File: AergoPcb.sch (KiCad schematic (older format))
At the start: 16 parts, among them SW1 SW_Push, U1 ATmega32U4-AU, Y1 16MHz

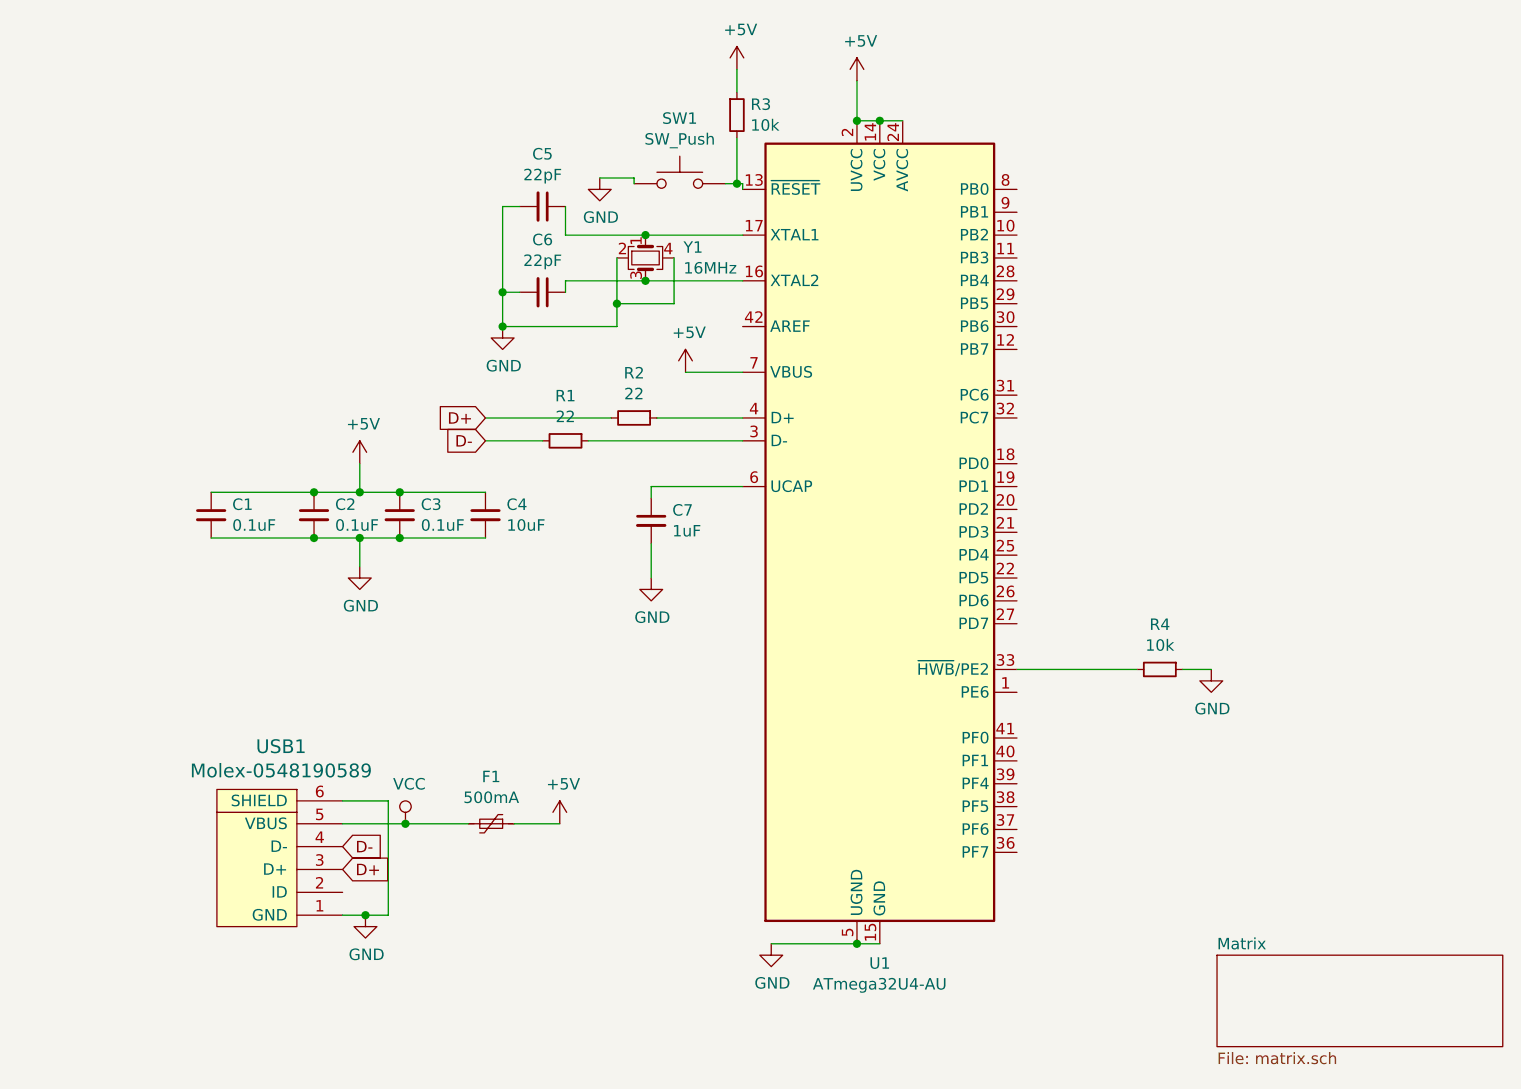
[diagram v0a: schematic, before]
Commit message: added jst footprints, continued work on pcb
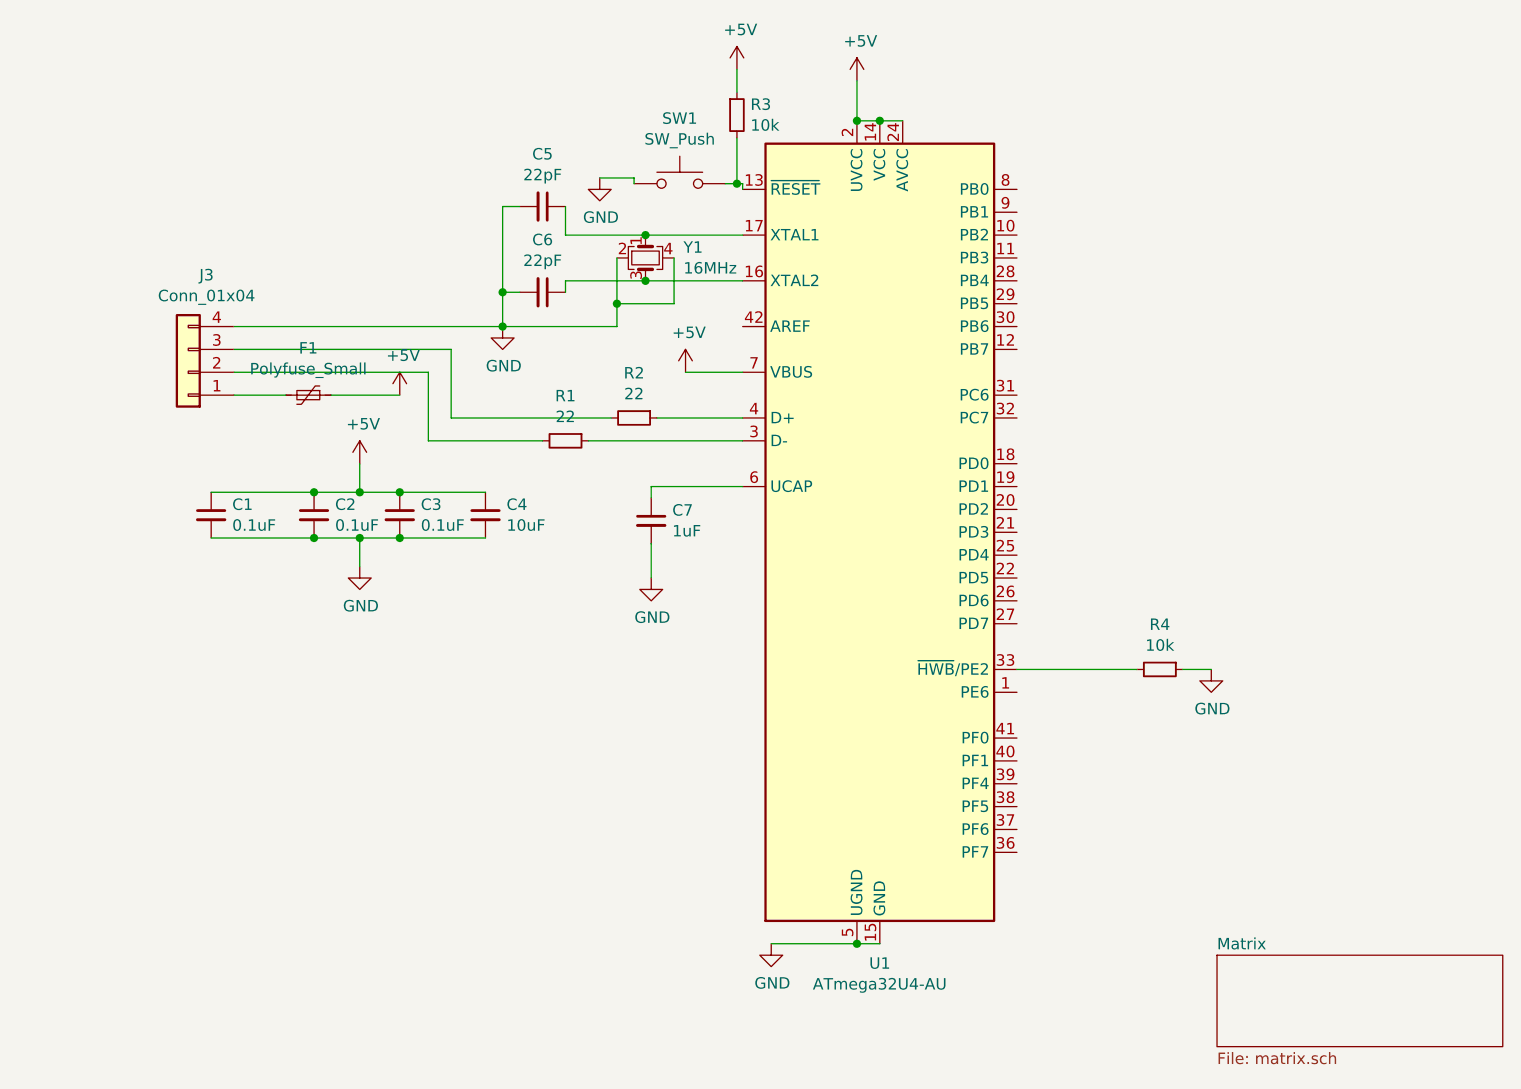
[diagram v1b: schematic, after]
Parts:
- removed USB1: Molex-0548190589, symbol random-keyboard-parts:Molex-0548190589
- added J3: Conn_01x04, symbol Connector_Generic:Conn_01x04
- C1, C2, C3, C4, C5, C6, C7: footprint (none) -> Capacitor_SMD:C_0805_2012Metric
- F1: value 500mA -> Polyfuse_Small
- R1, R2, R3, R4: footprint (none) -> Resistor_SMD:R_0805_2012Metric
- SW1: footprint (none) -> random-keyboard-parts:SKQG-1155865
- Y1: footprint (none) -> Crystal:Crystal_SMD_3225-4Pin_3.2x2.5mm
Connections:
- net GND: now also J3.4 (Pin_4)
- net D+: no longer names the net of R2.2
- net D+: now also J3.3 (Pin_3)
- net D-: no longer names the net of R1.2
- net D-: now also J3.2 (Pin_2)
- net VCC: no longer names the net of F1.2
- net VCC: now also J3.1 (Pin_1)
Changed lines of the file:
@@
 F 0 "R4" V 5329 4225 50  0000 C CNN
 F 1 "10k" V 5420 4225 50  0000 C CNN
-F 2 "" H 5525 4225 50  0001 C CNN
+F 2 "Resistor_SMD:R_0805_2012Metric" H 5525 4225 50  0001 C CNN
 F 3 "~" H 5525 4225 50  0001 C CNN
 	1    5525 4225
@@
 F 0 "R2" V 3029 3125 50  0000 C CNN
 F 1 "22" V 3120 3125 50  0000 C CNN
-F 2 "" H 3225 3125 50  0001 C CNN
+F 2 "Resistor_SMD:R_0805_2012Metric" H 3225 3125 50  0001 C CNN
 F 3 "~" H 3225 3125 50  0001 C CNN
 	1    3225 3125
@@
 F 0 "R1" V 2729 3225 50  0000 C CNN
 F 1 "22" V 2820 3225 50  0000 C CNN
-F 2 "" H 2925 3225 50  0001 C CNN
+F 2 "Resistor_SMD:R_0805_2012Metric" H 2925 3225 50  0001 C CNN
 F 3 "~" H 2925 3225 50  0001 C CNN
 	1    2925 3225
@@
 Wire Wire Line
 	3700 3125 3325 3125
-Wire Wire Line
-	2825 3225 2575 3225
-Wire Wire Line
-	3125 3125 2575 3125
 $Comp
 L Device:C_Small C7
@@
 F 0 "C7" H 3392 3621 50  0000 L CNN
 F 1 "1uF" H 3392 3530 50  0000 L CNN
-F 2 "" H 3300 3575 50  0001 C CNN
+F 2 "Capacitor_SMD:C_0805_2012Metric" H 3300 3575 50  0001 C CNN
 F 3 "~" H 3300 3575 50  0001 C CNN
 	1    3300 3575
@@
 F 0 "C1" H 1467 3596 50  0000 L CNN
 F 1 "0.1uF" H 1467 3505 50  0000 L CNN
-F 2 "" H 1375 3550 50  0001 C CNN
+F 2 "Capacitor_SMD:C_0805_2012Metric" H 1375 3550 50  0001 C CNN
 F 3 "~" H 1375 3550 50  0001 C CNN
 	1    1375 3550
@@
 F 0 "C2" H 1917 3596 50  0000 L CNN
 F 1 "0.1uF" H 1917 3505 50  0000 L CNN
-F 2 "" H 1825 3550 50  0001 C CNN
+F 2 "Capacitor_SMD:C_0805_2012Metric" H 1825 3550 50  0001 C CNN
 F 3 "~" H 1825 3550 50  0001 C CNN
 	1    1825 3550
@@
 F 0 "C3" H 2292 3596 50  0000 L CNN
 F 1 "0.1uF" H 2292 3505 50  0000 L CNN
-F 2 "" H 2200 3550 50  0001 C CNN
+F 2 "Capacitor_SMD:C_0805_2012Metric" H 2200 3550 50  0001 C CNN
 F 3 "~" H 2200 3550 50  0001 C CNN
 	1    2200 3550
@@
 F 0 "C4" H 2667 3596 50  0000 L CNN
 F 1 "10uF" H 2667 3505 50  0000 L CNN
-F 2 "" H 2575 3550 50  0001 C CNN
+F 2 "Capacitor_SMD:C_0805_2012Metric" H 2575 3550 50  0001 C CNN
 F 3 "~" H 2575 3550 50  0001 C CNN
 	1    2575 3550
@@
 Wire Wire Line
 	2025 3650 2200 3650
-Wire Wire Line
-	2025 3450 2025 3325
 Connection ~ 2025 3450
 Wire Wire Line
@@
 F 0 "Y1" V 3229 2591 50  0000 L CNN
 F 1 "16MHz" V 3320 2591 50  0000 L CNN
-F 2 "" H 3275 2425 50  0001 C CNN
+F 2 "Crystal:Crystal_SMD_3225-4Pin_3.2x2.5mm" H 3275 2425 50  0001 C CNN
 F 3 "~" H 3275 2425 50  0001 C CNN
 	1    3275 2425
@@
 F 0 "C5" V 2596 2200 50  0000 C CNN
 F 1 "22pF" V 2687 2200 50  0000 C CNN
-F 2 "" H 2825 2200 50  0001 C CNN
+F 2 "Capacitor_SMD:C_0805_2012Metric" H 2825 2200 50  0001 C CNN
 F 3 "~" H 2825 2200 50  0001 C CNN
 	1    2825 2200
@@
 F 0 "C6" V 2596 2575 50  0000 C CNN
 F 1 "22pF" V 2687 2575 50  0000 C CNN
-F 2 "" H 2825 2575 50  0001 C CNN
+F 2 "Capacitor_SMD:C_0805_2012Metric" H 2825 2575 50  0001 C CNN
 F 3 "~" H 2825 2575 50  0001 C CNN
 	1    2825 2575
@@
 F 0 "SW1" H 3425 2385 50  0000 C CNN
 F 1 "SW_Push" H 3425 2294 50  0000 C CNN
-F 2 "" H 3425 2300 50  0001 C CNN
+F 2 "random-keyboard-parts:SKQG-1155865" H 3425 2300 50  0001 C CNN
 F 3 "" H 3425 2300 50  0001 C CNN
 	1    3425 2100
@@
 F 0 "R3" H 3734 1846 50  0000 L CNN
 F 1 "10k" H 3734 1755 50  0000 L CNN
-F 2 "" H 3675 1800 50  0001 C CNN
+F 2 "Resistor_SMD:R_0805_2012Metric" H 3675 1800 50  0001 C CNN
 F 3 "~" H 3675 1800 50  0001 C CNN
 	1    3675 1800
@@
 	1    0    0    -1
 $EndComp
-Wire Wire Line
-	3675 1700 3675 1600
-Text GLabel 2575 3125 0    50   Input ~ 0
-D+
-Text GLabel 2575 3225 0    50   Input ~ 0
-D-
-$Comp
-L random-keyboard-parts:Molex-0548190589 USB1
-U 1 1 5C859DAB
-P 1650 5100
-F 0 "USB1" V 2187 5069 60  0000 C CNN
-F 1 "Molex-0548190589" V 2081 5069 60  0000 C CNN
-F 2 "" H 1650 5100 60  0001 C CNN
-F 3 "" H 1650 5100 60  0001 C CNN
-	1    1650 5100
-	0    -1   -1   0
-$EndComp
-$Comp
-L Device:Polyfuse_Small F1
-U 1 1 5C859EB2
-P 2600 4900
-F 0 "F1" V 2395 4900 50  0000 C CNN
-F 1 "500mA" V 2486 4900 50  0000 C CNN
-F 2 "" H 2650 4700 50  0001 L CNN
-F 3 "~" H 2600 4900 50  0001 C CNN
-	1    2600 4900
-	0    1    1    0
-$EndComp
-$Comp
-L power:VCC #PWR04
-U 1 1 5C85ABBD
-P 2225 4900
-F 0 "#PWR04" H 2225 4750 50  0001 C CNN
-F 1 "VCC" H 2242 5073 50  0000 C CNN
-F 2 "" H 2225 4900 50  0001 C CNN
-F 3 "" H 2225 4900 50  0001 C CNN
-	1    2225 4900
-	1    0    0    -1
-$EndComp
-$Comp
-L power:+5V #PWR06
-U 1 1 5C85AC52
-P 2900 4900
-F 0 "#PWR06" H 2900 4750 50  0001 C CNN
-F 1 "+5V" H 2915 5073 50  0000 C CNN
-F 2 "" H 2900 4900 50  0001 C CNN
-F 3 "" H 2900 4900 50  0001 C CNN
-	1    2900 4900
-	1    0    0    -1
-$EndComp
-Text GLabel 1950 5100 2    50   Input ~ 0
-D+
-Text GLabel 1950 5000 2    50   Input ~ 0
-D-
-Wire Wire Line
-	1950 4900 2225 4900
-Wire Wire Line
-	2225 4900 2500 4900
-Connection ~ 2225 4900
-Wire Wire Line
-	2700 4900 2900 4900
-$Comp
-L power:GND #PWR03
-U 1 1 5C85FBAF
-P 2050 5300
-F 0 "#PWR03" H 2050 5050 50  0001 C CNN
-F 1 "GND" H 2055 5127 50  0000 C CNN
-F 2 "" H 2050 5300 50  0001 C CNN
-F 3 "" H 2050 5300 50  0001 C CNN
-	1    2050 5300
-	1    0    0    -1
-$EndComp
-Wire Wire Line
-	1950 5300 2050 5300
 $Sheet
 S 5775 5475 1250 400
@@
 	1    0    0    -1
 $EndComp
-Wire Wire Line
-	1950 4800 2150 4800
-Wire Wire Line
-	2150 4800 2150 5300
-Wire Wire Line
-	2150 5300 2050 5300
-Connection ~ 2050 5300
+$Comp
+L Connector_Generic:Conn_01x04 J3
+U 1 1 5C95CF30
+P 1275 2925
+F 0 "J3" H 1195 2500 50  0000 C CNN
+F 1 "Conn_01x04" H 1195 2591 50  0000 C CNN
+F 2 "" H 1275 2925 50  0001 C CNN
+F 3 "~" H 1275 2925 50  0001 C CNN
+	1    1275 2925
+	-1   0    0    1
+$EndComp
+Wire Wire Line
+	2325 3225 2825 3225
+Wire Wire Line
+	3675 1600 3675 1700
+Wire Wire Line
+	2325 3225 2325 2925
+Wire Wire Line
+	2425 3125 2425 2825
+Wire Wire Line
+	2425 3125 3125 3125
+$Comp
+L Device:Polyfuse_Small F1
+U 1 1 5C9AFBD1
+P 1800 3025
+F 0 "F1" V 1595 3025 50  0000 C CNN
+F 1 "Polyfuse_Small" V 1686 3025 50  0000 C CNN
+F 2 "" H 1850 2825 50  0001 L CNN
+F 3 "~" H 1800 3025 50  0001 C CNN
+	1    1800 3025
+	0    1    1    0
+$EndComp
+Wire Wire Line
+	1475 2725 2650 2725
+Wire Wire Line
+	1475 2825 2425 2825
+Wire Wire Line
+	1475 2925 2325 2925
+Wire Wire Line
+	1475 3025 1700 3025
+Wire Wire Line
+	2025 3325 2025 3450
+$Comp
+L power:+5V #PWR0101
+U 1 1 5CBAF4D0
+P 2200 3025
+F 0 "#PWR0101" H 2200 2875 50  0001 C CNN
+F 1 "+5V" H 2215 3198 50  0000 C CNN
+F 2 "" H 2200 3025 50  0001 C CNN
+F 3 "" H 2200 3025 50  0001 C CNN
+	1    2200 3025
+	1    0    0    -1
+$EndComp
+Wire Wire Line
+	1900 3025 2200 3025
 $EndSCHEMATC

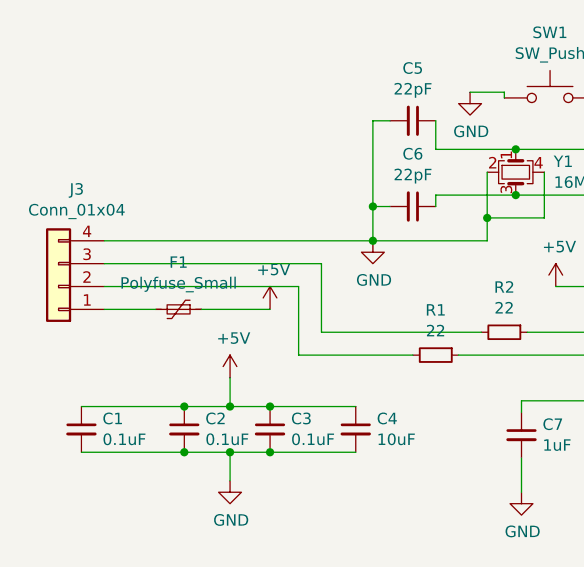
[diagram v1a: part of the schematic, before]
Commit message: finished right half, loaded keyboard parts pretty
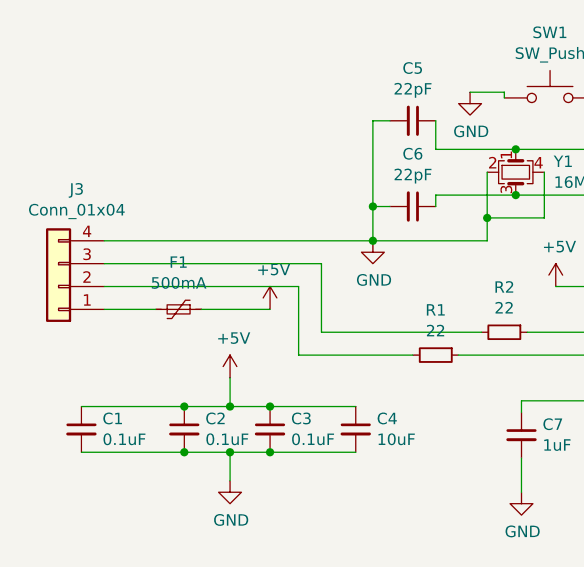
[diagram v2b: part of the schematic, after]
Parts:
- F1: value Polyfuse_Small -> 500mA; footprint (none) -> Fuse_Holders_and_Fuses:Fuse_SMD1206_Reflow
- J3: footprint (none) -> Connector_JST:JST_SH_SM04B-SRSS-TB_1x04-1MP_P1.00mm_Horizontal
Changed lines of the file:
@@
 F 0 "J3" H 1195 2500 50  0000 C CNN
 F 1 "Conn_01x04" H 1195 2591 50  0000 C CNN
-F 2 "" H 1275 2925 50  0001 C CNN
+F 2 "Connector_JST:JST_SH_SM04B-SRSS-TB_1x04-1MP_P1.00mm_Horizontal" H 1275 2925 50  0001 C CNN
 F 3 "~" H 1275 2925 50  0001 C CNN
 	1    1275 2925
@@
 P 1800 3025
 F 0 "F1" V 1595 3025 50  0000 C CNN
-F 1 "Polyfuse_Small" V 1686 3025 50  0000 C CNN
-F 2 "" H 1850 2825 50  0001 L CNN
+F 1 "500mA" V 1686 3025 50  0000 C CNN
+F 2 "Fuse_Holders_and_Fuses:Fuse_SMD1206_Reflow" H 1850 2825 50  0001 L CNN
 F 3 "~" H 1800 3025 50  0001 C CNN
 	1    1800 3025

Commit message: Finalized PCB and created Gerbers
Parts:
- added U2: PRTR5V0U2X, random-keyboard-parts:SOT143B, symbol 2019-04-04_07-10-47:PRTR5V0U2X
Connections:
- net GND: now also U2.1 (GND)
- net COL9: now reaches U1.10 (PB2)
- net COL8: now reaches U1.11 (PB3)
- net COL6: now reaches U1.19 (PD1)
- net SwLedPWM: now reaches U1.20 (PD2)
- net COL0: now reaches U1.21 (PD3)
- net ROW1: now reaches U1.22 (PD5)
- net ROW5: now reaches U1.25 (PD4)
- net COL1: now reaches U1.26 (PD6)
- net COL2: now reaches U1.27 (PD7)
- net COL3: now reaches U1.28 (PB4)
- net COL4: now reaches U1.29 (PB5)
- net D-: now reaches R1.1, U1.3 (D-)
- net ROW0: now reaches U1.30 (PB6)
- net COL5: now reaches U1.31 (PC6)
- net ROW4: now reaches U1.32 (PC7)
- net ROW3: now reaches U1.36 (PF7)
- net ROW2: now reaches U1.37 (PF6)
- net COL7: now reaches U1.38 (PF5)
- net COL13: now reaches U1.39 (PF4)
- net D+: now reaches R2.1, U1.4 (D+)
- net COL12: now reaches U1.40 (PF1)
- net COL11: now reaches U1.41 (PF0)
- net COL10: now reaches U1.9 (PB1)
- net at J3.3 (Pin_3), R2.2: now also U2.2 (I/O1)
- net at J3.2 (Pin_2), R1.2: now also U2.3 (I/O2)
- net at F1.2, J3.1 (Pin_1): now also U2.4 (VCC)
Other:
- moved on the sheet: R1, R2
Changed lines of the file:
@@
 L Device:R_Small R2
 U 1 1 5C80D3A9
-P 3225 3125
-F 0 "R2" V 3029 3125 50  0000 C CNN
-F 1 "22" V 3120 3125 50  0000 C CNN
-F 2 "Resistor_SMD:R_0805_2012Metric" H 3225 3125 50  0001 C CNN
-F 3 "~" H 3225 3125 50  0001 C CNN
-	1    3225 3125
+P 2040 2825
+F 0 "R2" V 1844 2825 50  0000 C CNN
+F 1 "22" V 1935 2825 50  0000 C CNN
+F 2 "Resistor_SMD:R_0805_2012Metric" H 2040 2825 50  0001 C CNN
+F 3 "~" H 2040 2825 50  0001 C CNN
+	1    2040 2825
 	0    1    1    0
 $EndComp
@@
 L Device:R_Small R1
 U 1 1 5C80D430
-P 2925 3225
-F 0 "R1" V 2729 3225 50  0000 C CNN
-F 1 "22" V 2820 3225 50  0000 C CNN
-F 2 "Resistor_SMD:R_0805_2012Metric" H 2925 3225 50  0001 C CNN
-F 3 "~" H 2925 3225 50  0001 C CNN
-	1    2925 3225
-	0    1    1    0
-$EndComp
-Wire Wire Line
-	3700 3225 3025 3225
-Wire Wire Line
-	3700 3125 3325 3125
+P 2040 2925
+F 0 "R1" V 1844 2925 50  0000 C CNN
+F 1 "22" V 1935 2925 50  0000 C CNN
+F 2 "Resistor_SMD:R_0805_2012Metric" H 2040 2925 50  0001 C CNN
+F 3 "~" H 2040 2925 50  0001 C CNN
+	1    2040 2925
+	0    1    1    0
+$EndComp
 $Comp
 L Device:C_Small C7
@@
 $EndComp
 Wire Wire Line
-	2325 3225 2825 3225
-Wire Wire Line
 	3675 1600 3675 1700
-Wire Wire Line
-	2325 3225 2325 2925
-Wire Wire Line
-	2425 3125 2425 2825
-Wire Wire Line
-	2425 3125 3125 3125
 $Comp
 L Device:Polyfuse_Small F1
@@
 	1475 2725 2650 2725
 Wire Wire Line
-	1475 2825 2425 2825
-Wire Wire Line
-	1475 2925 2325 2925
-Wire Wire Line
-	1475 3025 1700 3025
+	1475 3025 1585 3025
 Wire Wire Line
 	2025 3325 2025 3450
@@
 L power:+5V #PWR0101
 U 1 1 5CBAF4D0
-P 2200 3025
-F 0 "#PWR0101" H 2200 2875 50  0001 C CNN
-F 1 "+5V" H 2215 3198 50  0000 C CNN
-F 2 "" H 2200 3025 50  0001 C CNN
-F 3 "" H 2200 3025 50  0001 C CNN
-	1    2200 3025
-	1    0    0    -1
-$EndComp
-Wire Wire Line
-	1900 3025 2200 3025
+P 2430 3025
+F 0 "#PWR0101" H 2430 2875 50  0001 C CNN
+F 1 "+5V" H 2445 3198 50  0000 C CNN
+F 2 "" H 2430 3025 50  0001 C CNN
+F 3 "" H 2430 3025 50  0001 C CNN
+	1    2430 3025
+	1    0    0    -1
+$EndComp
+Text GLabel 4900 2425 2    50   Input ~ 0
+COL8
+Text GLabel 4900 2325 2    50   Input ~ 0
+COL9
+Text GLabel 4900 2225 2    50   Input ~ 0
+COL10
+Text GLabel 4900 4525 2    50   Input ~ 0
+COL11
+Text GLabel 4900 4625 2    50   Input ~ 0
+COL12
+Text GLabel 4900 4725 2    50   Input ~ 0
+COL13
+Text GLabel 4900 4825 2    50   Input ~ 0
+COL7
+Text GLabel 4900 4925 2    50   Input ~ 0
+ROW2
+Text GLabel 4900 5025 2    50   Input ~ 0
+ROW3
+Text GLabel 4900 3725 2    50   Input ~ 0
+ROW5
+Text GLabel 4900 3125 2    50   Input ~ 0
+ROW4
+Text GLabel 4900 3025 2    50   Input ~ 0
+COL5
+Text GLabel 4900 2725 2    50   Input ~ 0
+ROW0
+Text GLabel 4900 3925 2    50   Input ~ 0
+COL1
+Text GLabel 4900 2525 2    50   Input ~ 0
+COL3
+Text GLabel 4900 2625 2    50   Input ~ 0
+COL4
+Text GLabel 4900 4025 2    50   Input ~ 0
+COL2
+Text GLabel 4900 3825 2    50   Input ~ 0
+ROW1
+Text GLabel 4900 3625 2    50   Input ~ 0
+COL0
+Text GLabel 4900 3525 2    50   Input ~ 0
+SwLedPWM
+Text GLabel 4900 3425 2    50   Input ~ 0
+COL6
+$Comp
+L 2019-04-04_07-10-47:PRTR5V0U2X U2
+U 1 1 5CA5BEBF
+P 1190 4710
+F 0 "U2" H 2390 5097 60  0000 C CNN
+F 1 "PRTR5V0U2X" H 2390 4991 60  0000 C CNN
+F 2 "random-keyboard-parts:SOT143B" H 2390 4950 60  0001 C CNN
+F 3 "" H 1190 4710 60  0000 C CNN
+	1    1190 4710
+	1    0    0    -1
+$EndComp
+$Comp
+L power:GND #PWR0102
+U 1 1 5CA5EE38
+P 730 4710
+F 0 "#PWR0102" H 730 4460 50  0001 C CNN
+F 1 "GND" H 735 4537 50  0000 C CNN
+F 2 "" H 730 4710 50  0001 C CNN
+F 3 "" H 730 4710 50  0001 C CNN
+	1    730  4710
+	1    0    0    -1
+$EndComp
+Wire Wire Line
+	1190 4710 730  4710
+Wire Wire Line
+	1475 2925 1525 2925
+Wire Wire Line
+	1475 2825 1610 2825
+Text GLabel 2140 2825 2    50   Input ~ 0
+D+
+Text GLabel 2140 2925 2    50   Input ~ 0
+D-
+Wire Wire Line
+	1900 3025 2430 3025
+Wire Wire Line
+	1585 3025 1585 3280
+Wire Wire Line
+	1585 3280 1150 3280
+Wire Wire Line
+	1150 3280 1150 4185
+Wire Wire Line
+	1150 4185 3590 4185
+Wire Wire Line
+	3590 4185 3590 4710
+Connection ~ 1585 3025
+Wire Wire Line
+	1585 3025 1700 3025
+Text GLabel 3700 3125 0    50   Input ~ 0
+D+
+Text GLabel 3700 3225 0    50   Input ~ 0
+D-
+Wire Wire Line
+	1610 2825 1610 2770
+Wire Wire Line
+	1610 2770 595  2770
+Wire Wire Line
+	595  2770 595  4950
+Wire Wire Line
+	595  4950 1190 4950
+Wire Wire Line
+	1190 4950 1190 4810
+Connection ~ 1610 2825
+Wire Wire Line
+	1610 2825 1940 2825
+Wire Wire Line
+	3590 4810 3590 5030
+Wire Wire Line
+	3590 5030 530  5030
+Wire Wire Line
+	530  5030 530  3165
+Wire Wire Line
+	530  3165 1525 3165
+Wire Wire Line
+	1525 3165 1525 2925
+Connection ~ 1525 2925
+Wire Wire Line
+	1525 2925 1940 2925
 $EndSCHEMATC
